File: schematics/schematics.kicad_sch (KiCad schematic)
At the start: 9 parts, among them Q1 S8050, Q2 S8050

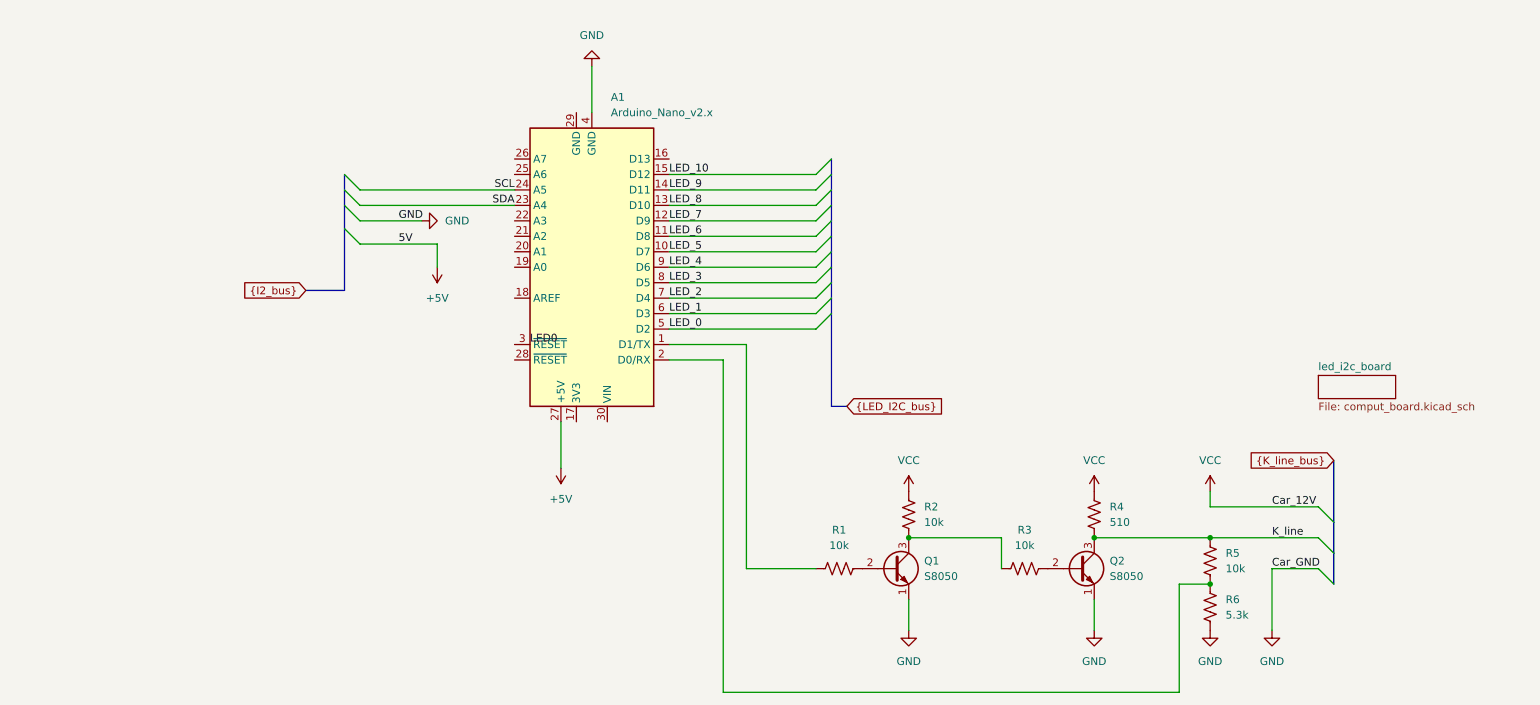
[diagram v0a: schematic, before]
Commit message: added subschimatics
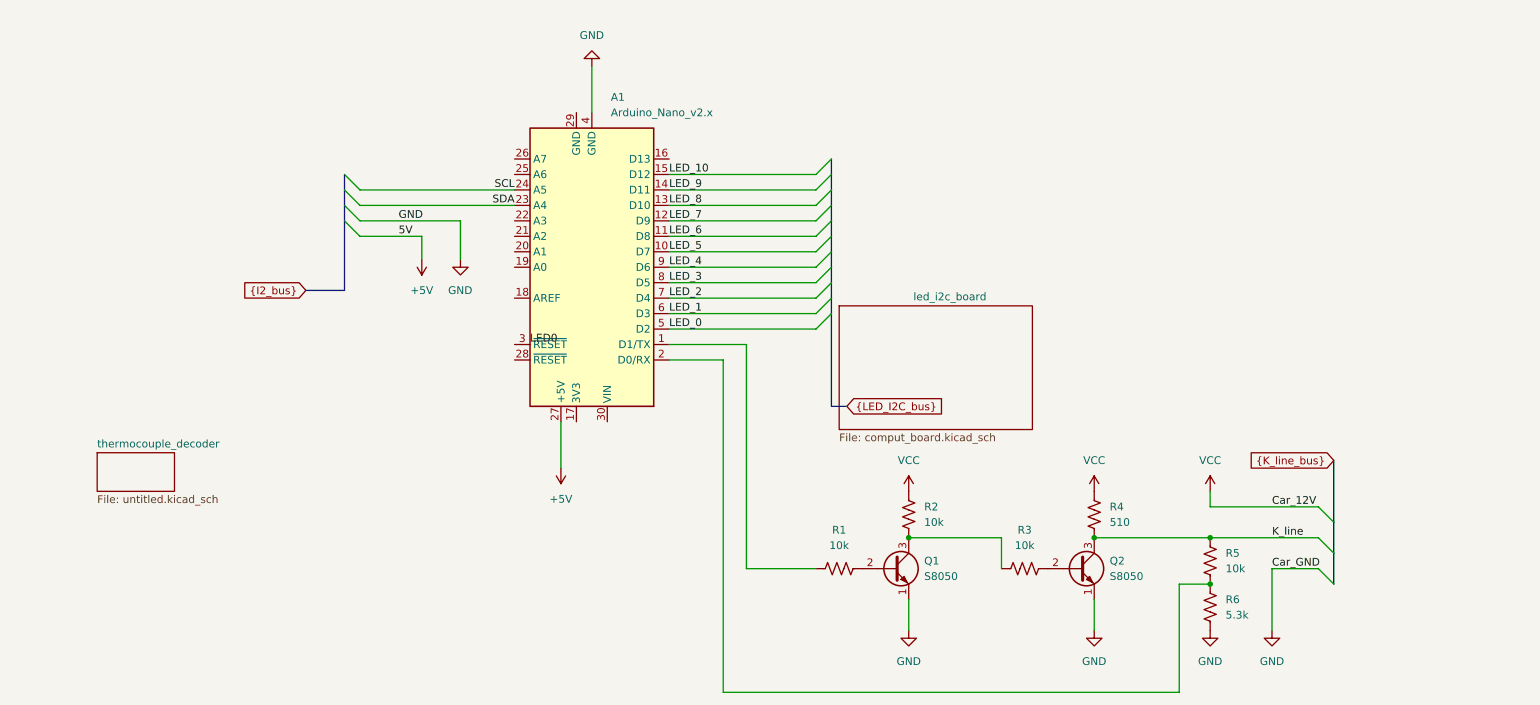
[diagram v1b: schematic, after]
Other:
- added sheet thermocouple_decoder (untitled.kicad_sch)
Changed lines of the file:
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@@
 	)
 	(bus_entry
-		(at 100.33 91.44)
+		(at 100.33 90.17)
 		(size 2.54 2.54)
 		(stroke
@@
 	(wire
 		(pts
-			(xy 102.87 90.17) (xy 113.03 90.17)
-		)
-		(stroke
-			(width 0)
-			(type default)
-		)
-	)
-	(wire
-		(pts
 			(xy 223.52 157.48) (xy 223.52 152.4)
 		)
@@
 	(wire
 		(pts
-			(xy 102.87 93.98) (xy 115.57 93.98)
+			(xy 102.87 92.71) (xy 113.03 92.71)
+		)
+		(stroke
+			(width 0)
+			(type default)
+		)
+	)
+	(wire
+		(pts
+			(xy 119.38 90.17) (xy 119.38 96.52)
 		)
 		(stroke
@@
 	(bus
 		(pts
-			(xy 100.33 87.63) (xy 100.33 91.44)
+			(xy 100.33 87.63) (xy 100.33 90.17)
 		)
 		(stroke
@@
 	(wire
 		(pts
-			(xy 115.57 93.98) (xy 115.57 97.79)
+			(xy 113.03 92.71) (xy 113.03 96.52)
 		)
 		(stroke
@@
 	(bus
 		(pts
-			(xy 100.33 91.44) (xy 100.33 101.6)
+			(xy 100.33 90.17) (xy 100.33 101.6)
 		)
 		(stroke
@@
 		(pts
 			(xy 162.56 113.03) (xy 153.67 113.03)
+		)
+		(stroke
+			(width 0)
+			(type default)
+		)
+	)
+	(wire
+		(pts
+			(xy 119.38 90.17) (xy 102.87 90.17)
 		)
 		(stroke
@@
 	)
 	(label "5V"
-		(at 109.22 93.98 0)
+		(at 109.22 92.71 0)
 		(effects
 			(font
@@
 	(symbol
 		(lib_id "power:GND")
-		(at 113.03 90.17 90)
+		(at 119.38 96.52 0)
 		(unit 1)
 		(exclude_from_sim no)
@@
 		(on_board yes)
 		(dnp no)
-		(fields_autoplaced yes)
 		(property "Reference" "#PWR09"
-			(at 119.38 90.17 0)
+			(at 119.38 102.87 0)
 			(effects
 				(font
@@
 		)
 		(property "Value" "GND"
-			(at 116.84 90.1699 90)
-			(effects
-				(font
-					(size 1.27 1.27)
-				)
-				(justify right)
+			(at 117.348 101.6 0)
+			(effects
+				(font
+					(size 1.27 1.27)
+				)
+				(justify left)
 			)
 		)
 		(property "Footprint" ""
-			(at 113.03 90.17 0)
+			(at 119.38 96.52 0)
 			(effects
 				(font
@@
 		)
 		(property "Datasheet" ""
-			(at 113.03 90.17 0)
+			(at 119.38 96.52 0)
 			(effects
 				(font
@@
 		)
 		(property "Description" "Power symbol creates a global label with name \"GND\" , ground"
-			(at 113.03 90.17 0)
+			(at 119.38 96.52 0)
 			(effects
 				(font
@@
 	(symbol
 		(lib_id "power:+5V")
-		(at 115.57 97.79 180)
+		(at 113.03 96.52 180)
 		(unit 1)
 		(exclude_from_sim no)
@@
 		(fields_autoplaced yes)
 		(property "Reference" "#PWR010"
-			(at 115.57 93.98 0)
+			(at 113.03 92.71 0)
 			(effects
 				(font
@@
 		)
 		(property "Value" "+5V"
-			(at 115.57 102.87 0)
+			(at 113.03 101.6 0)
 			(effects
 				(font
@@
 		)
 		(property "Footprint" ""
-			(at 115.57 97.79 0)
+			(at 113.03 96.52 0)
 			(effects
 				(font
@@
 		)
 		(property "Datasheet" ""
-			(at 115.57 97.79 0)
+			(at 113.03 96.52 0)
 			(effects
 				(font
@@
 		)
 		(property "Description" "Power symbol creates a global label with name \"+5V\""
-			(at 115.57 97.79 0)
+			(at 113.03 96.52 0)
 			(effects
 				(font
@@
 	)
 	(sheet
-		(at 260.35 115.57)
-		(size 12.7 3.81)
+		(at 181.61 104.14)
+		(size 31.75 20.32)
+		(exclude_from_sim no)
+		(in_bom yes)
+		(on_board yes)
+		(dnp no)
+		(stroke
+			(width 0.1524)
+			(type solid)
+		)
+		(fill
+			(color 0 0 0 0.0000)
+		)
+		(property "Sheetname" "led_i2c_board"
+			(at 193.802 103.378 0)
+			(effects
+				(font
+					(size 1.27 1.27)
+				)
+				(justify left bottom)
+			)
+		)
+		(property "Sheetfile" "comput_board.kicad_sch"
+			(at 181.61 125.0446 0)
+			(effects
+				(font
+					(size 1.27 1.27)
+				)
+				(justify left top)
+			)
+		)
+		(instances
+			(project "schematics"
+				(path "/7fd7cdd6-b1c2-42a7-9276-fecd452b4132"
+					(page "2")
+				)
+			)
+		)
+	)
+	(sheet
+		(at 59.69 128.27)
+		(size 12.7 6.35)
 		(exclude_from_sim no)
 		(in_bom yes)
@@
 			(color 0 0 0 0.0000)
 		)
-		(property "Sheetname" "led_i2c_board"
-			(at 260.35 114.8584 0)
+		(property "Sheetname" "thermocouple_decoder"
+			(at 59.69 127.5584 0)
 			(effects
 				(font
@@
 			)
 		)
-		(property "Sheetfile" "comput_board.kicad_sch"
-			(at 260.35 119.9646 0)
+		(property "Sheetfile" "untitled.kicad_sch"
+			(at 59.69 135.2046 0)
 			(effects
 				(font
@@
 			(project "schematics"
 				(path "/7fd7cdd6-b1c2-42a7-9276-fecd452b4132"
-					(page "2")
-				)
-			)
+					(page "3")
+				)
+			)

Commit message: mostly done with the sub-schematics
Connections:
- net PWM_output: now reaches A1.19 (A0)
- net Tone_genorator: now reaches A1.20 (A1)

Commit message: finished compute board
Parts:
- added C2: 0.22u, symbol Device:C
- added U3: ~, Package_TO_SOT_THT:TO-220-3_Vertical, symbol LM340AT:LM340AT
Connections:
- net GND: now also C2.2, U3. (GND)
- net VCC: now also C2.1, U3.1 (Vin)
- net at A1.30 (VIN): now also U3.3 (Out)

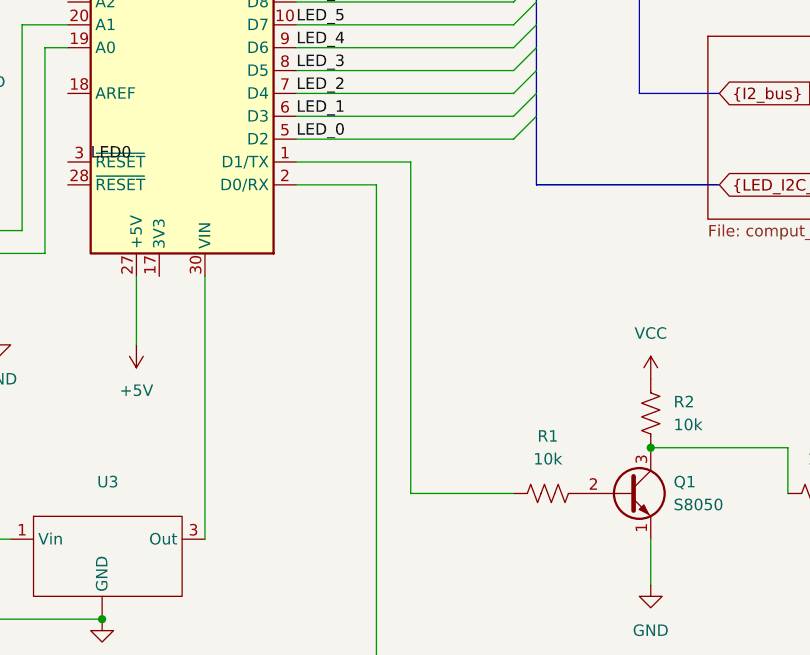
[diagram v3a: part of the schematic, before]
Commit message: added titles to all sheets
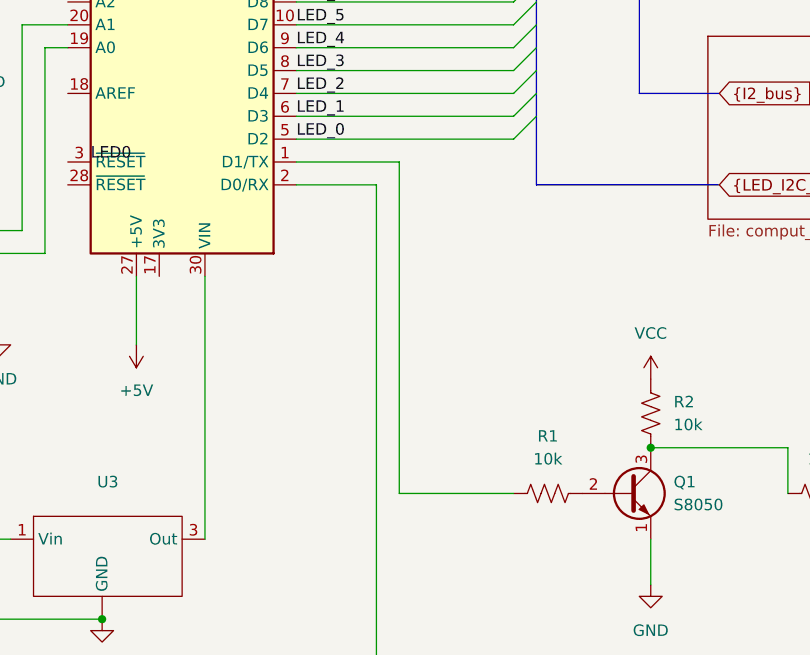
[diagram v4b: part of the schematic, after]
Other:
- company: (none) -> wish4snow
- title: (none) -> Compute Board
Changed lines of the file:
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@@
 	(generator_version "9.0")
 	(paper "USLetter")
+	(title_block
+		(title "Compute Board")
+		(date "2026-01-22")
+		(rev "1")
+		(company "wish4snow")
+	)
 	(bus_alias "I2_bus"
 		(members "5V" "GND" "SDA" "SCL")
@@
 	(wire
 		(pts
-			(xy 166.37 110.49) (xy 166.37 147.32)
+			(xy 165.1 110.49) (xy 165.1 147.32)
 		)
 		(stroke
@@
 	(wire
 		(pts
-			(xy 166.37 147.32) (xy 177.8 147.32)
+			(xy 165.1 147.32) (xy 177.8 147.32)
 		)
 		(stroke
@@
 	(wire
 		(pts
-			(xy 153.67 110.49) (xy 166.37 110.49)
-		)
-		(stroke
+			(xy 153.67 110.49) (xy 165.1 110.49)
+		)
+		(stroke

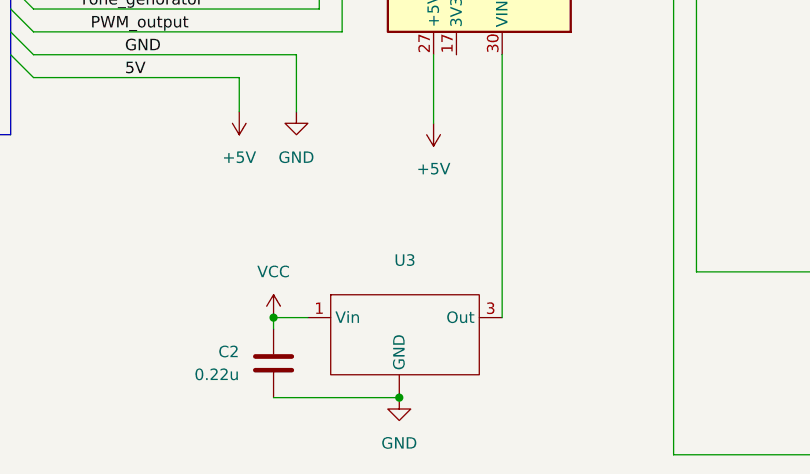
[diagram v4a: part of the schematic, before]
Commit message: added valve for LM340AT
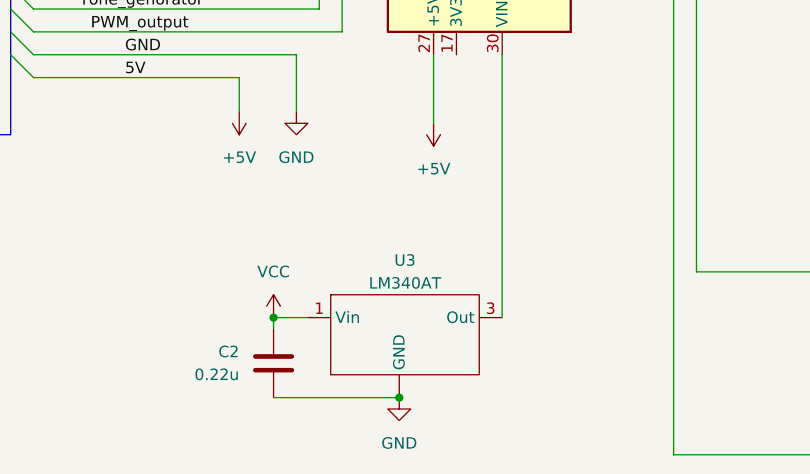
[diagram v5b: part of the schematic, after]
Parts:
- U3: value ~ -> LM340AT
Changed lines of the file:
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@@
 			)
 		)
-		(property "Value" "~"
+		(property "Value" "LM340AT"
 			(at 132.715 148.59 0)
 			(effects

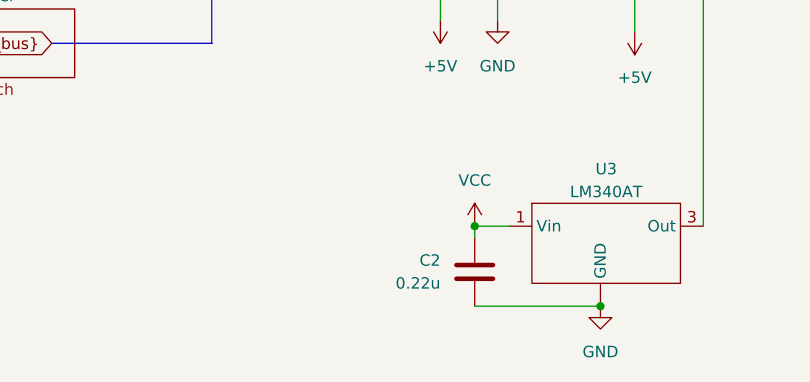
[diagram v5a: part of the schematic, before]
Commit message: fixed and added values to schematics
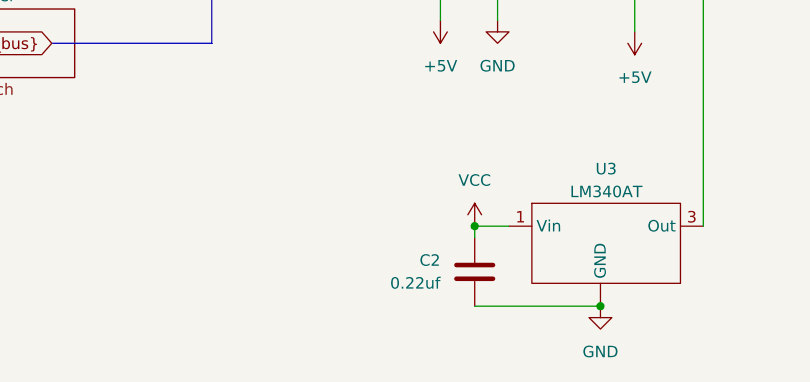
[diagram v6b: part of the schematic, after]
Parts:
- C2: value 0.22u -> 0.22uf
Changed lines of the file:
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@@
 			)
 		)
-		(property "Value" "0.22u"
+		(property "Value" "0.22uf"
 			(at 114.3 158.7499 0)
 			(effects
